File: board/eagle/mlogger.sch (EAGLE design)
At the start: 42 parts, among them J1 MICROSD-9P, SW1 SS-12D00G3, SW2 TVAF06-A020B-R, SW3 TVAF06-A020B-R

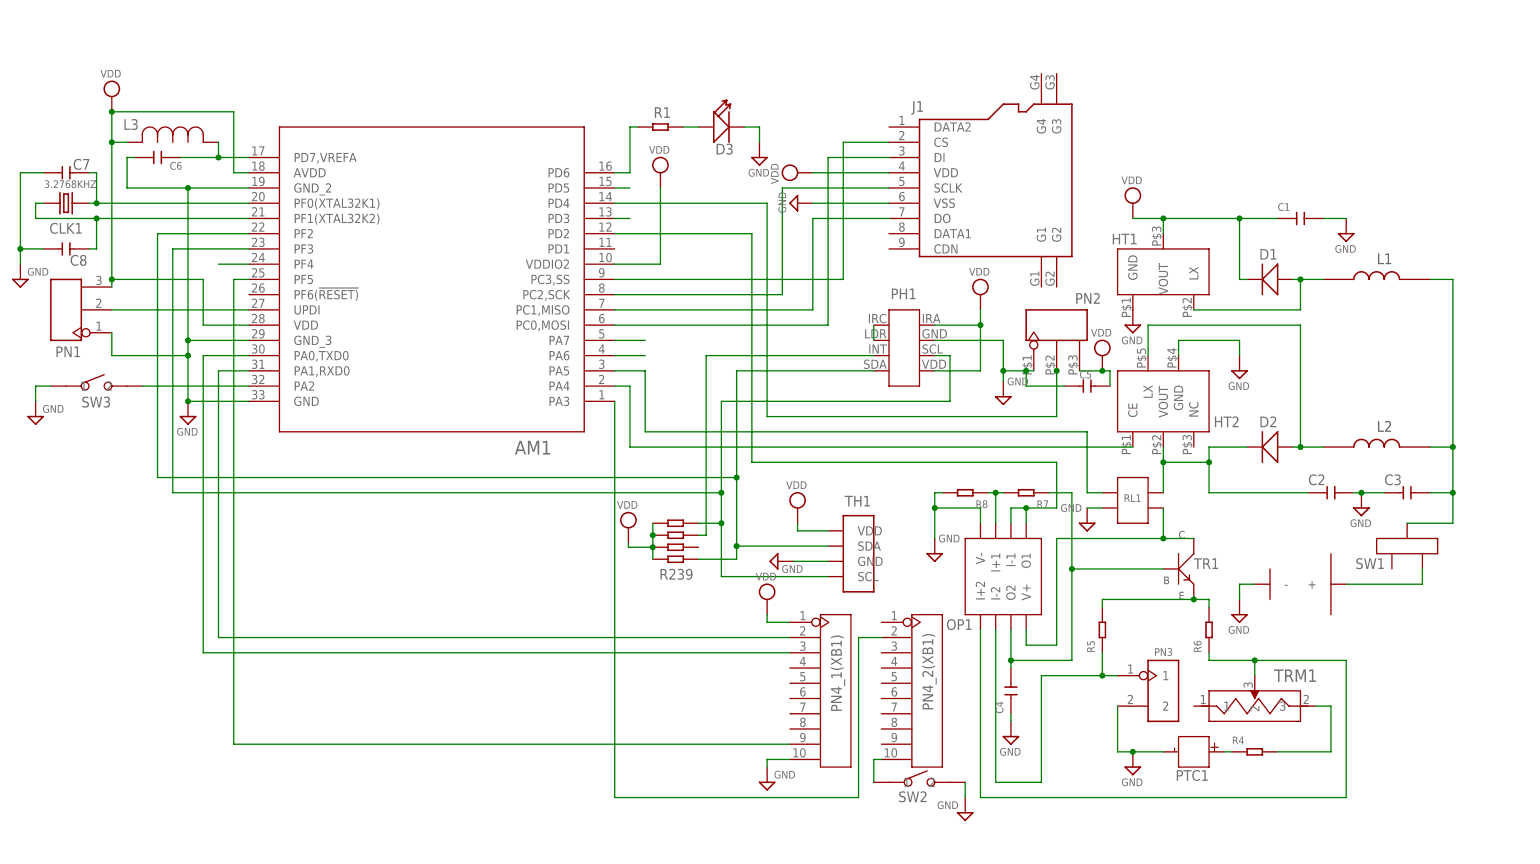
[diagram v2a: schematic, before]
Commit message: 電源スイッチ位置の改良。 外部水晶発振子の設定修正。 風速センサ起動ピンの修正。 USARTのRXピンをプルアップ。 XBeeスリープのタイミングをmainメソッドに移行。
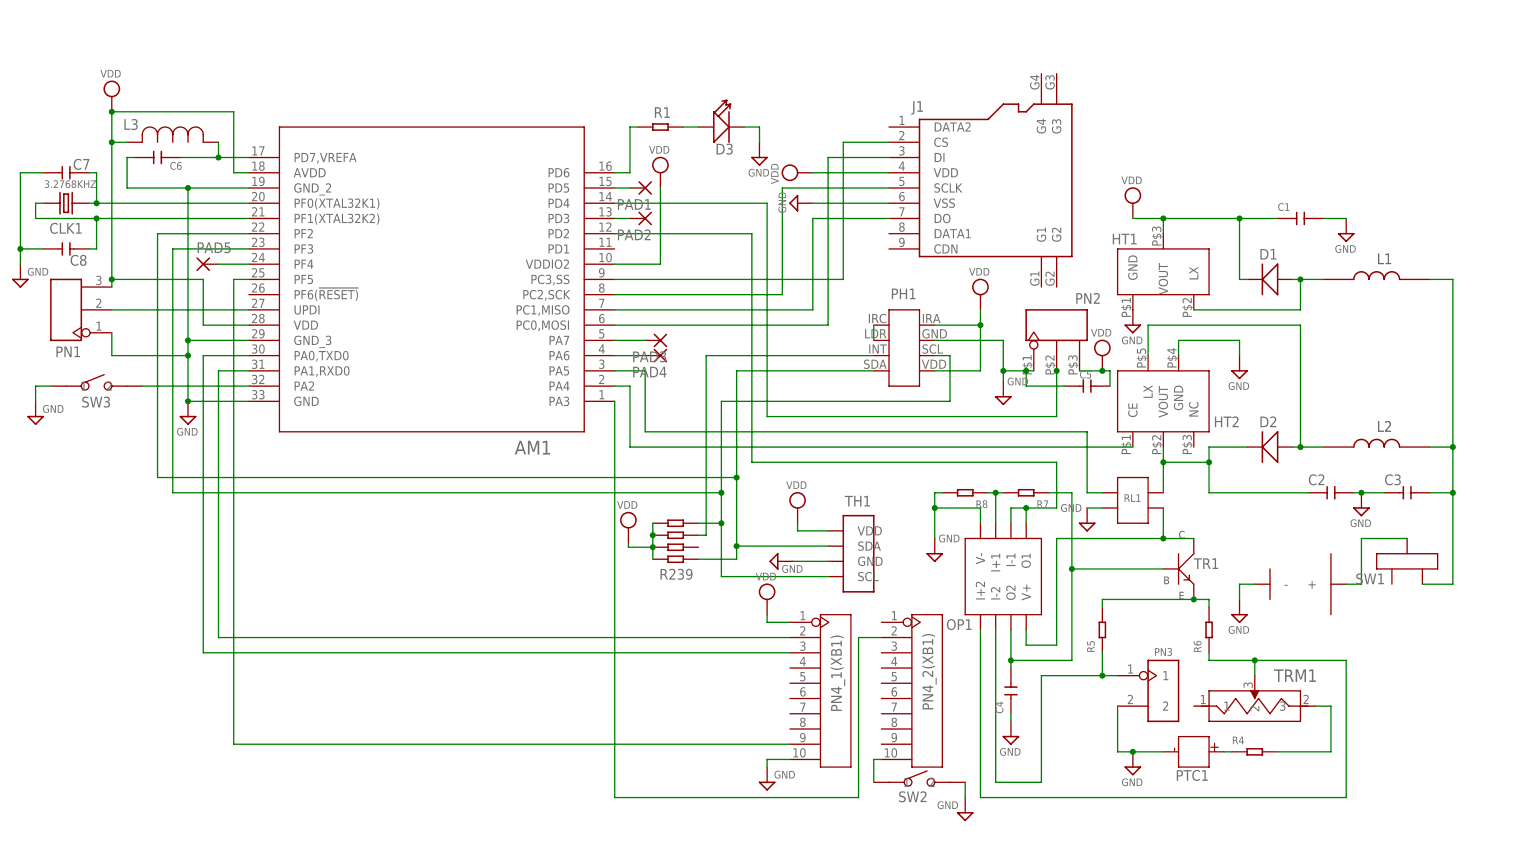
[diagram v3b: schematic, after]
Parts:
- added PAD1, PAD2, PAD3, PAD4, PAD5: (no value), wirepad:1,6/0,8
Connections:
- removed net VBT: BB1.+, SW1.P1
- new net N$14: BB1.+, SW1.P2
- net N$11: now also PAD1.P
- net N$12: now also PAD3.P
- net N$13: now also PAD4.P
- net N$8: now also PAD2.P
- net N$9: now also PAD5.P
- net P$11: now also SW1.P1; no longer SW1.P2
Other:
- moved on the sheet: SW1
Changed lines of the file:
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@@
 <part name="C8" library="MyParts" deviceset="MURATA_0603" device="" package3d_urn="urn:adsk.eagle:package:8004287/1"/>
 <part name="SUPPLY1" library="supply2" library_urn="urn:adsk.eagle:library:372" deviceset="GND" device=""/>
+<part name="PAD1" library="wirepad" library_urn="urn:adsk.eagle:library:412" deviceset="1,6/0,8" device="" package3d_urn="urn:adsk.eagle:package:30830/1"/>
+<part name="PAD2" library="wirepad" library_urn="urn:adsk.eagle:library:412" deviceset="1,6/0,8" device="" package3d_urn="urn:adsk.eagle:package:30830/1"/>
+<part name="PAD3" library="wirepad" library_urn="urn:adsk.eagle:library:412" deviceset="1,6/0,8" device="" package3d_urn="urn:adsk.eagle:package:30830/1"/>
+<part name="PAD4" library="wirepad" library_urn="urn:adsk.eagle:library:412" deviceset="1,6/0,8" device="" package3d_urn="urn:adsk.eagle:package:30830/1"/>
+<part name="PAD5" library="wirepad" library_urn="urn:adsk.eagle:library:412" deviceset="1,6/0,8" device="" package3d_urn="urn:adsk.eagle:package:30830/1"/>
 </parts>
 <sheets>
@@
 <attribute name="NAME" x="6.604" y="-23.622" size="1.778" layer="95" ratio="10"/>
 </instance>
-<instance part="SW1" gate="G$1" x="91.44" y="15.24" smashed="yes">
-<attribute name="NAME" x="82.804" y="15.24" size="1.778" layer="95"/>
+<instance part="SW1" gate="G$1" x="91.44" y="12.7" smashed="yes">
+<attribute name="NAME" x="82.804" y="12.7" size="1.778" layer="95"/>
 </instance>
 <instance part="R239" gate="G$1" x="-30.48" y="22.86" smashed="yes">
@@
 <instance part="SUPPLY1" gate="GND" x="-139.7" y="63.5" smashed="yes">
 <attribute name="VALUE" x="-138.557" y="64.135" size="1.27" layer="96"/>
+</instance>
+<instance part="PAD1" gate="P" x="-35.56" y="78.74" smashed="yes" rot="R180">
+<attribute name="NAME" x="-34.417" y="76.8858" size="1.778" layer="95" rot="R180"/>
+<attribute name="VALUE" x="-34.417" y="82.042" size="1.778" layer="96" rot="R180"/>
+</instance>
+<instance part="PAD2" gate="P" x="-35.56" y="73.66" smashed="yes" rot="R180">
+<attribute name="NAME" x="-34.417" y="71.8058" size="1.778" layer="95" rot="R180"/>
+<attribute name="VALUE" x="-34.417" y="76.962" size="1.778" layer="96" rot="R180"/>
+</instance>
+<instance part="PAD3" gate="P" x="-33.02" y="53.34" smashed="yes" rot="R180">
+<attribute name="NAME" x="-31.877" y="51.4858" size="1.778" layer="95" rot="R180"/>
+<attribute name="VALUE" x="-31.877" y="56.642" size="1.778" layer="96" rot="R180"/>
+</instance>
+<instance part="PAD4" gate="P" x="-33.02" y="50.8" smashed="yes" rot="R180">
+<attribute name="NAME" x="-31.877" y="48.9458" size="1.778" layer="95" rot="R180"/>
+<attribute name="VALUE" x="-31.877" y="54.102" size="1.778" layer="96" rot="R180"/>
+</instance>
+<instance part="PAD5" gate="P" x="-109.22" y="66.04" smashed="yes">
+<attribute name="NAME" x="-110.363" y="67.8942" size="1.778" layer="95"/>
+<attribute name="VALUE" x="-110.363" y="62.738" size="1.778" layer="96"/>
 </instance>
 </instances>
@@
 <pinref part="L2" gate="G$1" pin="P$2"/>
 <pinref part="C3" gate="G$1" pin="2"/>
-<pinref part="SW1" gate="G$1" pin="P2"/>
-<wire x1="91.44" y1="22.86" x2="99.06" y2="22.86" width="0.1524" layer="91"/>
-<wire x1="99.06" y1="22.86" x2="99.06" y2="27.94" width="0.1524" layer="91"/>
 <junction x="99.06" y="27.94"/>
+<pinref part="SW1" gate="G$1" pin="P1"/>
+<wire x1="93.98" y1="12.7" x2="99.06" y2="12.7" width="0.1524" layer="91"/>
+<wire x1="99.06" y1="12.7" x2="99.06" y2="27.94" width="0.1524" layer="91"/>
 </segment>
 </net>
@@
 <pinref part="PH1" gate="G$1" pin="INT"/>
 <wire x1="2.54" y1="50.8" x2="-25.4" y2="50.8" width="0.1524" layer="91"/>
-</segment>
-</net>
-<net name="VBT" class="0">
-<segment>
-<pinref part="BB1" gate="G$1" pin="+"/>
-<pinref part="SW1" gate="G$1" pin="P1"/>
-<wire x1="81.28" y1="12.7" x2="93.98" y2="12.7" width="0.1524" layer="91"/>
-<wire x1="93.98" y1="12.7" x2="93.98" y2="15.24" width="0.1524" layer="91"/>
 </segment>
 </net>
@@
 <pinref part="AM1" gate="A" pin="PF4"/>
 <wire x1="-101.6" y1="66.04" x2="-106.68" y2="66.04" width="0.1524" layer="91"/>
+<pinref part="PAD5" gate="P" pin="P"/>
 </segment>
 </net>
@@
 <pinref part="AM1" gate="A" pin="PD3"/>
 <wire x1="-40.64" y1="73.66" x2="-38.1" y2="73.66" width="0.1524" layer="91"/>
+<pinref part="PAD2" gate="P" pin="P"/>
 </segment>
 </net>
@@
 <pinref part="AM1" gate="A" pin="PD5"/>
 <wire x1="-40.64" y1="78.74" x2="-38.1" y2="78.74" width="0.1524" layer="91"/>
+<pinref part="PAD1" gate="P" pin="P"/>
 </segment>
 </net>
@@
 <pinref part="AM1" gate="A" pin="PA7"/>
 <wire x1="-40.64" y1="53.34" x2="-35.56" y2="53.34" width="0.1524" layer="91"/>
+<pinref part="PAD3" gate="P" pin="P"/>
 </segment>
 </net>
@@
 <pinref part="AM1" gate="A" pin="PA6"/>
 <wire x1="-40.64" y1="50.8" x2="-35.56" y2="50.8" width="0.1524" layer="91"/>
-</segment>
-</net>
+<pinref part="PAD4" gate="P" pin="P"/>
+</segment>
+</net>
+<net name="N$14" class="0">
+<segment>
+<pinref part="BB1" gate="G$1" pin="+"/>
+<wire x1="81.28" y1="12.7" x2="83.82" y2="12.7" width="0.1524" layer="91"/>
+<wire x1="83.82" y1="12.7" x2="83.82" y2="20.32" width="0.1524" layer="91"/>
+<pinref part="SW1" gate="G$1" pin="P2"/>
+<wire x1="83.82" y1="20.32" x2="91.44" y2="20.32" width="0.1524" layer="91"/>
+</segment>
+</net>

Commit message: UPDI, GAD名称設定。 ノイズ対策で配線間隔を拡大。
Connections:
- net N$11 renamed GADC2
- net N$7 renamed UPDI
- net N$8 renamed GADC3
- net N$9 renamed GADC1
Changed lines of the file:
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@@
 </segment>
 </net>
-<net name="N$7" class="0">
+<net name="UPDI" class="0">
 <segment>
 <pinref part="PN1" gate="G$1" pin="P$2"/>
@@
 </segment>
 </net>
-<net name="N$9" class="0">
+<net name="GADC1" class="0">
 <segment>
 <pinref part="AM1" gate="A" pin="PF4"/>
@@
 </segment>
 </net>
-<net name="N$8" class="0">
+<net name="GADC3" class="0">
 <segment>
 <pinref part="AM1" gate="A" pin="PD3"/>
@@
 </segment>
 </net>
-<net name="N$11" class="0">
+<net name="GADC2" class="0">
 <segment>
 <pinref part="AM1" gate="A" pin="PD5"/>

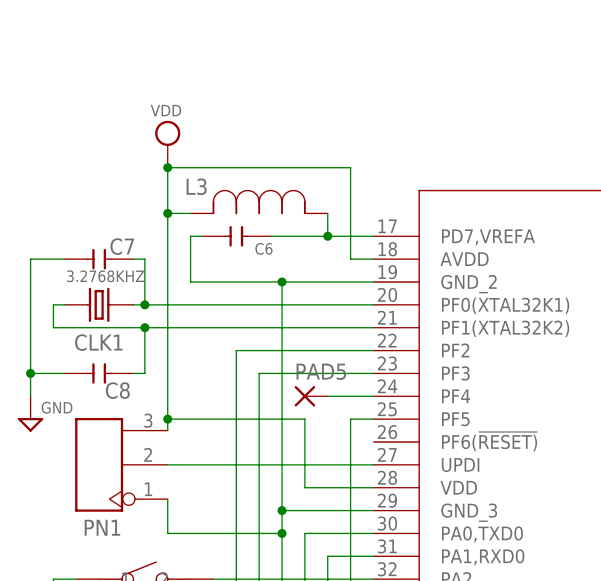
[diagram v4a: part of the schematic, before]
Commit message: アナログReference電圧に三端子レギュレータ回路を追加。
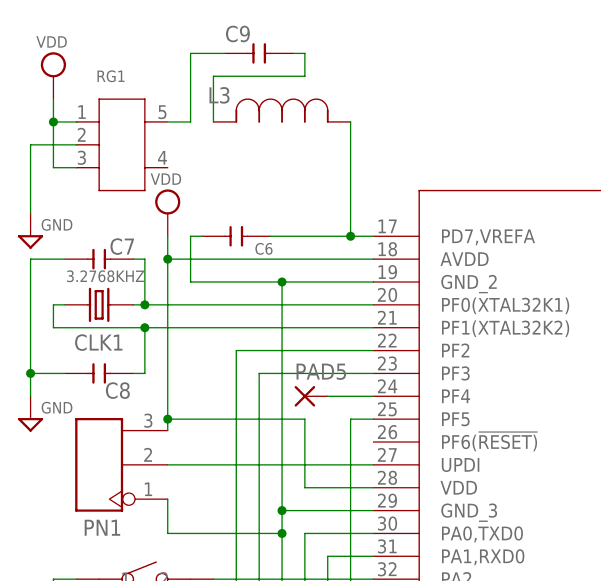
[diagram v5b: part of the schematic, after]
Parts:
- added C9: (no value), MyParts:MURATA_0603
- added RG1: TCR2EF20SOT-25___(SMV)_TOS, MyParts:TCR2EF20SOT-25___(SMV)_TOS
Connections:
- new net N$7: C9.2, L3.2
- new net N$9: C9.1, RG1.5
- net GND: now also RG1.2
- net VDD: now also RG1.1, RG1.3; no longer L3.2
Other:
- moved on the sheet: L3
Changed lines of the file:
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@@
 <part name="PAD4" library="wirepad" library_urn="urn:adsk.eagle:library:412" deviceset="1,6/0,8" device="" package3d_urn="urn:adsk.eagle:package:30830/1"/>
 <part name="PAD5" library="wirepad" library_urn="urn:adsk.eagle:library:412" deviceset="1,6/0,8" device="" package3d_urn="urn:adsk.eagle:package:30830/1"/>
+<part name="RG1" library="MyParts" deviceset="TCR2EF20" device="SOT-25___(SMV)_TOS"/>
+<part name="SUPPLY6" library="supply2" library_urn="urn:adsk.eagle:library:372" deviceset="GND" device=""/>
+<part name="SUPPLY10" library="supply2" library_urn="urn:adsk.eagle:library:372" deviceset="VDD" device=""/>
+<part name="C9" library="MyParts" deviceset="MURATA_0603" device="" package3d_urn="urn:adsk.eagle:package:8004287/1"/>
 </parts>
 <sheets>
@@
 <attribute name="VALUE" x="-12.065" y="28.575" size="1.27" layer="96"/>
 </instance>
-<instance part="SUPPLY13" gate="G$1" x="-124.46" y="93.98" smashed="yes">
-<attribute name="VALUE" x="-126.365" y="97.155" size="1.27" layer="96"/>
+<instance part="SUPPLY13" gate="G$1" x="-124.46" y="86.36" smashed="yes">
+<attribute name="VALUE" x="-126.365" y="89.535" size="1.27" layer="96"/>
 </instance>
 <instance part="CLK1" gate="G$1" x="-132.08" y="76.2" smashed="yes" rot="R180">
@@
 <attribute name="VALUE" x="-34.925" y="84.455" size="1.27" layer="96"/>
 </instance>
-<instance part="L3" gate="A" x="-121.92" y="86.36" smashed="yes">
-<attribute name="NAME" x="-122.5758" y="88.4301" size="1.778" layer="95" ratio="10"/>
+<instance part="L3" gate="A" x="-119.38" y="96.52" smashed="yes">
+<attribute name="NAME" x="-120.0358" y="98.5901" size="1.778" layer="95" ratio="10"/>
 </instance>
 <instance part="TRM1" gate="A" x="58.42" y="-10.16" smashed="yes">
@@
 <attribute name="NAME" x="-110.363" y="67.8942" size="1.778" layer="95"/>
 <attribute name="VALUE" x="-110.363" y="62.738" size="1.778" layer="96"/>
+</instance>
+<instance part="RG1" gate="A" x="-132.08" y="99.06" smashed="yes">
+<attribute name="NAME" x="-132.4213" y="100.965" size="1.27" layer="95" ratio="6"/>
+</instance>
+<instance part="SUPPLY6" gate="GND" x="-139.7" y="83.82" smashed="yes">
+<attribute name="VALUE" x="-138.557" y="84.455" size="1.27" layer="96"/>
+</instance>
+<instance part="SUPPLY10" gate="G$1" x="-137.16" y="101.6" smashed="yes">
+<attribute name="VALUE" x="-139.065" y="104.775" size="1.27" layer="96"/>
+</instance>
+<instance part="C9" gate="G$1" x="-114.3" y="104.14" smashed="yes">
+<attribute name="NAME" x="-118.11" y="105.41" size="1.778" layer="95" ratio="10"/>
+<attribute name="VALUE" x="-118.11" y="101.6" size="1.27" layer="96" ratio="10"/>
 </instance>
 </instances>
@@
 <junction x="-139.7" y="68.58"/>
 </segment>
+<segment>
+<pinref part="SUPPLY6" gate="GND" pin="GND"/>
+<wire x1="-139.7" y1="93.98" x2="-139.7" y2="86.36" width="0.1524" layer="91"/>
+<pinref part="RG1" gate="A" pin="2"/>
+<wire x1="-134.5946" y1="93.98" x2="-139.7" y2="93.98" width="0.1524" layer="91"/>
+</segment>
 </net>
 <net name="VDD" class="2">
@@
 <wire x1="-109.22" y1="63.5" x2="-124.46" y2="63.5" width="0.1524" layer="91"/>
 <junction x="-124.46" y="63.5"/>
-<wire x1="-124.46" y1="91.44" x2="-124.46" y2="86.36" width="0.1524" layer="91"/>
+<wire x1="-124.46" y1="83.82" x2="-124.46" y2="81.28" width="0.1524" layer="91"/>
 <pinref part="AM1" gate="A" pin="AVDD"/>
-<wire x1="-124.46" y1="86.36" x2="-124.46" y2="63.5" width="0.1524" layer="91"/>
-<wire x1="-101.6" y1="81.28" x2="-104.14" y2="81.28" width="0.1524" layer="91"/>
-<wire x1="-104.14" y1="81.28" x2="-104.14" y2="91.44" width="0.1524" layer="91"/>
-<wire x1="-104.14" y1="91.44" x2="-124.46" y2="91.44" width="0.1524" layer="91"/>
-<junction x="-124.46" y="91.44"/>
-<pinref part="L3" gate="A" pin="2"/>
-<wire x1="-121.92" y1="86.36" x2="-124.46" y2="86.36" width="0.1524" layer="91"/>
-<junction x="-124.46" y="86.36"/>
+<wire x1="-124.46" y1="81.28" x2="-124.46" y2="63.5" width="0.1524" layer="91"/>
+<wire x1="-101.6" y1="81.28" x2="-124.46" y2="81.28" width="0.1524" layer="91"/>
+<junction x="-124.46" y="81.28"/>
 </segment>
 <segment>
@@
 <pinref part="SUPPLY3" gate="G$1" pin="VDD"/>
 <wire x1="-33.02" y1="66.04" x2="-33.02" y2="78.74" width="0.1524" layer="91"/>
+</segment>
+<segment>
+<pinref part="RG1" gate="A" pin="1"/>
+<pinref part="SUPPLY10" gate="G$1" pin="VDD"/>
+<wire x1="-134.5946" y1="96.52" x2="-137.16" y2="96.52" width="0.1524" layer="91"/>
+<wire x1="-137.16" y1="96.52" x2="-137.16" y2="99.06" width="0.1524" layer="91"/>
+<wire x1="-137.16" y1="91.44" x2="-137.16" y2="96.52" width="0.1524" layer="91"/>
+<junction x="-137.16" y="96.52"/>
+<pinref part="RG1" gate="A" pin="3"/>
+<wire x1="-134.5946" y1="91.44" x2="-137.16" y2="91.44" width="0.1524" layer="91"/>
 </segment>
 </net>
@@
 <net name="VREFA" class="0">
 <segment>
-<wire x1="-113.03" y1="83.82" x2="-106.68" y2="83.82" width="0.1524" layer="91"/>
-<wire x1="-106.68" y1="83.82" x2="-106.68" y2="86.36" width="0.1524" layer="91"/>
+<wire x1="-113.03" y1="83.82" x2="-104.14" y2="83.82" width="0.1524" layer="91"/>
+<wire x1="-104.14" y1="83.82" x2="-104.14" y2="96.52" width="0.1524" layer="91"/>
 <pinref part="C6" gate="G$1" pin="2"/>
 <pinref part="AM1" gate="A" pin="PD7,VREFA"/>
-<wire x1="-101.6" y1="83.82" x2="-106.68" y2="83.82" width="0.1524" layer="91"/>
-<junction x="-106.68" y="83.82"/>
+<wire x1="-101.6" y1="83.82" x2="-104.14" y2="83.82" width="0.1524" layer="91"/>
+<junction x="-104.14" y="83.82"/>
 <pinref part="L3" gate="A" pin="1"/>
 </segment>
@@
 </segment>
 </net>
+<net name="N$7" class="0">
+<segment>
+<pinref part="L3" gate="A" pin="2"/>
+<pinref part="C9" gate="G$1" pin="2"/>
+<wire x1="-110.49" y1="104.14" x2="-109.22" y2="104.14" width="0.1524" layer="91"/>
+<wire x1="-109.22" y1="104.14" x2="-109.22" y2="101.6" width="0.1524" layer="91"/>
+<wire x1="-109.22" y1="101.6" x2="-119.38" y2="101.6" width="0.1524" layer="91"/>
+<wire x1="-119.38" y1="101.6" x2="-119.38" y2="96.52" width="0.1524" layer="91"/>
+</segment>
+</net>
+<net name="N$9" class="0">
+<segment>
+<pinref part="C9" gate="G$1" pin="1"/>
+<pinref part="RG1" gate="A" pin="5"/>
+<wire x1="-124.4346" y1="96.52" x2="-121.92" y2="96.52" width="0.1524" layer="91"/>
+<wire x1="-121.92" y1="96.52" x2="-121.92" y2="104.14" width="0.1524" layer="91"/>
+<wire x1="-121.92" y1="104.14" x2="-118.11" y2="104.14" width="0.1524" layer="91"/>
+</segment>
+</net>
